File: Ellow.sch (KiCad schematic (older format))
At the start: 24 parts, among them J1 USB_C_Receptacle_USB2.0, J2 M_2_AKey_KB, J3 Conn_01x02_Female, Q1 A03407, Q2 A03407, U1 AP2112K-3.3, U2 E73-2G4M08S1C, U3 LN2054Y42AMR, Y1 32.768kHz

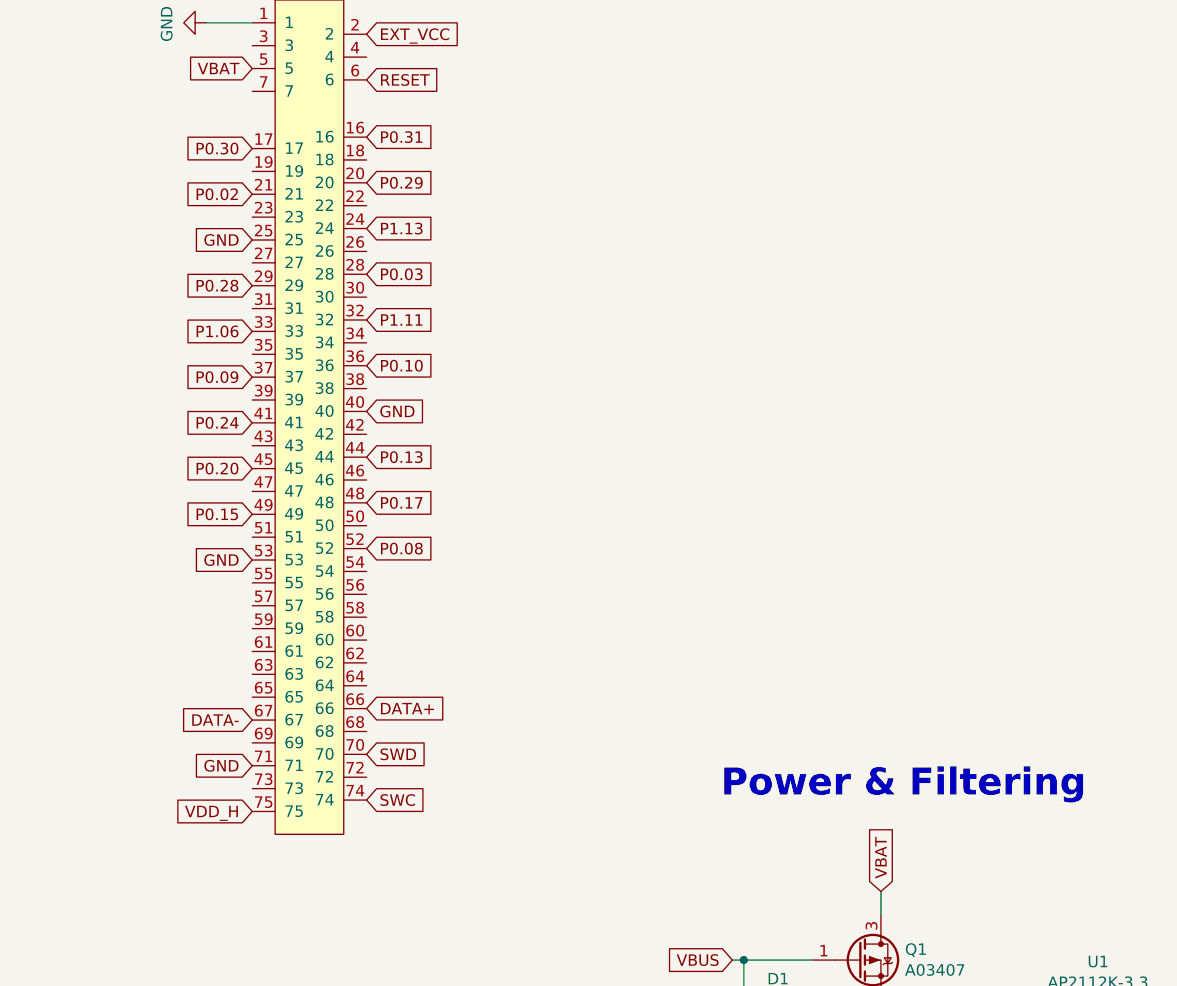
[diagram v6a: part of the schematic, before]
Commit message: no routing solution yet
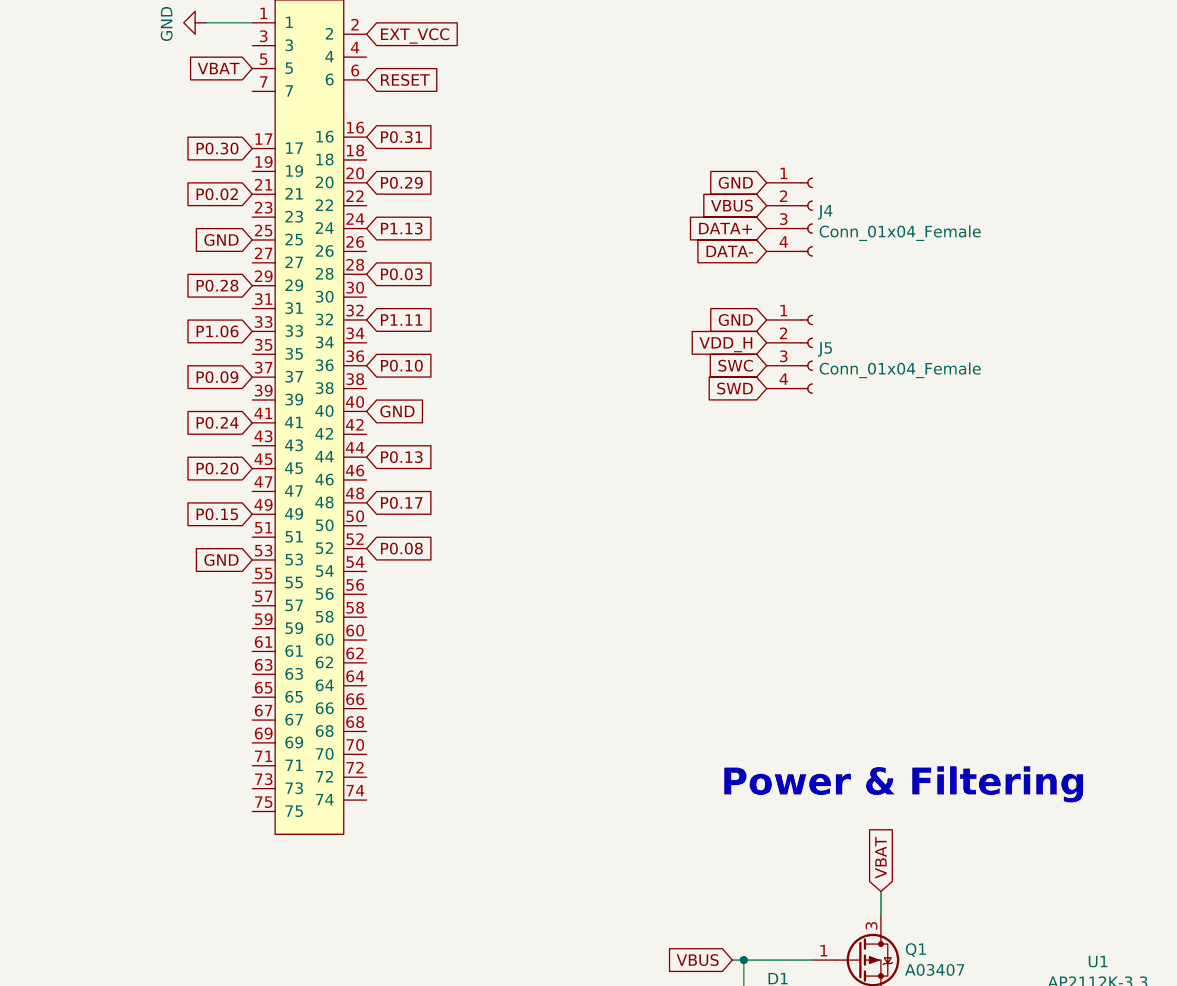
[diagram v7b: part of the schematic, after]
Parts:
- added J4, J5: Conn_01x04_Female, Connector_PinHeader_2.54mm:PinHeader_1x04_P2.54mm_Vertical, symbol Connector:Conn_01x04_Female
- J3: footprint Connector_PinHeader_1.27mm:PinHeader_1x02_P1.27mm_Vertical -> Connector_PinHeader_2.54mm:PinHeader_1x02_P2.54mm_Vertical
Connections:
- net DATA+: now also J4.3 (Pin_3); no longer J2.66
- net DATA-: now also J4.4 (Pin_4); no longer J2.67
- net GND: now also J4.1 (Pin_1), J5.1 (Pin_1); no longer J2.71
- net SWC: now also J5.3 (Pin_3); no longer J2.74
- net SWD: now also J5.4 (Pin_4); no longer J2.70
- net VBUS: now also J4.2 (Pin_2)
- net VDD_H: now also J5.2 (Pin_2); no longer J2.75
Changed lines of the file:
@@
 F 0 "J3" H 7428 6076 50  0000 L CNN
 F 1 "Conn_01x02_Female" H 7428 5985 50  0000 L CNN
-F 2 "Connector_PinHeader_1.27mm:PinHeader_1x02_P1.27mm_Vertical" H 7400 6100 50  0001 C CNN
+F 2 "Connector_PinHeader_2.54mm:PinHeader_1x02_P2.54mm_Vertical" H 7400 6100 50  0001 C CNN
 F 3 "~" H 7400 6100 50  0001 C CNN
 	1    7400 6100
@@
 Text GLabel 7150 3500 2    50   Input ~ 0
 P0.08
-Text GLabel 6650 4450 0    50   Input ~ 0
+Text GLabel 8900 2500 0    50   Input ~ 0
 GND
 Text GLabel 6650 3550 0    50   Input ~ 0
 GND
-Text GLabel 6650 4650 0    50   Input ~ 0
+Text GLabel 8900 2600 0    50   Input ~ 0
 VDD_H
-Text GLabel 7150 4600 2    50   Input ~ 0
+Text GLabel 8900 2700 0    50   Input ~ 0
 SWC
-Text GLabel 7150 4400 2    50   Input ~ 0
+Text GLabel 8900 2800 0    50   Input ~ 0
 SWD
-Text GLabel 7150 4200 2    50   Input ~ 0
+Text GLabel 8900 2100 0    50   Input ~ 0
 DATA+
-Text GLabel 6650 4250 0    50   Input ~ 0
+Text GLabel 8900 2200 0    50   Input ~ 0
 DATA-
 Text GLabel 3600 5500 2    50   Input ~ 0
@@
 Wire Wire Line
 	1750 6650 1800 6650
+$Comp
+L Connector:Conn_01x04_Female J5
+U 1 1 5FDB4AEC
+P 9100 2600
+F 0 "J5" H 9128 2576 50  0000 L CNN
+F 1 "Conn_01x04_Female" H 9128 2485 50  0000 L CNN
+F 2 "Connector_PinHeader_2.54mm:PinHeader_1x04_P2.54mm_Vertical" H 9100 2600 50  0001 C CNN
+F 3 "~" H 9100 2600 50  0001 C CNN
+	1    9100 2600
+	1    0    0    -1
+$EndComp
+$Comp
+L Connector:Conn_01x04_Female J4
+U 1 1 5FDB58A8
+P 9100 2000
+F 0 "J4" H 9128 1976 50  0000 L CNN
+F 1 "Conn_01x04_Female" H 9128 1885 50  0000 L CNN
+F 2 "Connector_PinHeader_2.54mm:PinHeader_1x04_P2.54mm_Vertical" H 9100 2000 50  0001 C CNN
+F 3 "~" H 9100 2000 50  0001 C CNN
+	1    9100 2000
+	1    0    0    -1
+$EndComp
+Text GLabel 8900 1900 0    50   Input ~ 0
+GND
+Text GLabel 8900 2000 0    50   Input ~ 0
+VBUS
 $EndSCHEMATC

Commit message: prelim routing
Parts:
- J4, J5: footprint Connector_PinHeader_2.54mm:PinHeader_1x04_P2.54mm_Vertical -> ellow:PinHeader_1x04_P2.54mm_Vertical_small
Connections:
- net BATTERY_MEASURE: now also U2.8 (P0.29/AIN5); no longer U2.18 (P0.04/AIN2)
- net EXT_VCC_CONTROL: now also U2.9 (P0.31/AIN7); no longer U2.17 (P1.09)
- net GND: now also J2.16, J2.17; no longer J2.25, J2.40, J2.53
- net P0.02: no longer J2.21
- net P0.03: no longer J2.28
- net P0.08: no longer J2.52
- net P0.09: now also J2.70; no longer J2.37
- net P0.10: now also J2.74; no longer J2.36
- net P0.13: now also J2.54; no longer J2.44
- net P0.15: now also J2.47; no longer J2.49
- net P0.17: now also J2.51; no longer J2.48
- net P0.20: now also J2.55; no longer J2.45
- net P0.22: now also J2.59
- net P0.24: now also J2.58; no longer J2.41
- net P0.28: no longer J2.29
- net P1.00: now also J2.63
- net P1.02: now also J2.67
- net P1.04: now also J2.71
- net P1.06: now also J2.75; no longer J2.33
- net P1.11: no longer J2.32
- net P1.13: no longer J2.24
- net PROG: now also U2.10 (P0.30/AIN6); no longer U2.15 (P0.05/AIN3)
- net RESET: now also J2.42; no longer J2.6
- net SWC: now also J5.4 (Pin_4); no longer J5.3 (Pin_3)
- net SWD: now also J5.3 (Pin_3); no longer J5.4 (Pin_4)
- net at U2.2 (P1.10): no longer D3.2 (A)
- net 90.07 renamed P0.07
- net P0.07: now also D3.2 (A)
- net P0.29: no longer names the net of J2.20
- net P0.29: no longer U2.8 (P0.29/AIN5)
- removed net P0.30: J2.17, U2.10 (P0.30/AIN6)
- removed net P0.31: J2.16, U2.9 (P0.31/AIN7)
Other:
- moved on the sheet: D3, R9
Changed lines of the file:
@@
 Text GLabel 2550 4250 1    50   Input ~ 0
 VDD_H
-Text GLabel 2650 4250 1    50   Input ~ 0
+Text GLabel 3600 5600 2    50   Input ~ 0
 BATTERY_MEASURE
-Text GLabel 2750 4250 1    50   Input ~ 0
+Text GLabel 3600 5500 2    50   Input ~ 0
 EXT_VCC_CONTROL
-Text GLabel 2950 4250 1    50   Input ~ 0
+Text GLabel 3600 5400 2    50   Input ~ 0
 PROG
-Wire Wire Line
-	2950 4350 2950 4250
-Wire Wire Line
-	2750 4350 2750 4250
-Wire Wire Line
-	2650 4400 2650 4250
 Wire Wire Line
 	2550 4350 2550 4250
@@
 	6650 1200 6450 1200
 $Comp
-L Device:LED D3
-U 1 1 5FC73EC6
-P 4150 6200
-F 0 "D3" H 4143 6417 50  0000 C CNN
-F 1 "LED" H 4143 6326 50  0000 C CNN
-F 2 "LED_SMD:LED_0603_1608Metric" H 4150 6200 50  0001 C CNN
-F 3 "~" H 4150 6200 50  0001 C CNN
-	1    4150 6200
-	-1   0    0    1
-$EndComp
-$Comp
-L Device:R_Small R9
-U 1 1 5FC73ECC
-P 4450 6200
-F 0 "R9" V 4254 6200 50  0000 C CNN
-F 1 "10k" V 4345 6200 50  0000 C CNN
-F 2 "Resistor_SMD:R_0603_1608Metric_Pad0.98x0.95mm_HandSolder" H 4450 6200 50  0001 C CNN
-F 3 "~" H 4450 6200 50  0001 C CNN
-	1    4450 6200
-	0    -1   -1   0
-$EndComp
-Wire Wire Line
-	4300 6200 4350 6200
-$Comp
-L power:GND #PWR0114
-U 1 1 5FC76B15
-P 4650 6200
-F 0 "#PWR0114" H 4650 5950 50  0001 C CNN
-F 1 "GND" H 4655 6027 50  0000 C CNN
-F 2 "" H 4650 6200 50  0001 C CNN
-F 3 "" H 4650 6200 50  0001 C CNN
-	1    4650 6200
-	1    0    0    -1
-$EndComp
-Wire Wire Line
-	4550 6200 4650 6200
-$Comp
 L Mechanical:MountingHole H1
 U 1 1 5FCBB591
@@
 Text Notes 6550 5900 0    118  ~ 24
 Battery Connection
-Wire Wire Line
-	3600 6200 4000 6200
 Wire Wire Line
 	3600 5900 4650 5900
@@
 Text GLabel 3600 5700 2    50   Input ~ 0
 P0.02
-Text GLabel 3600 5600 2    50   Input ~ 0
-P0.29
-Text GLabel 7150 1450 2    50   Input ~ 0
+Text GLabel 7150 3000 2    50   Input ~ 0
 RESET
 Text GLabel 7150 1250 2    50   Input ~ 0
 EXT_VCC
 Text GLabel 6650 1750 0    50   Input ~ 0
-P0.30
-Text GLabel 7150 1700 2    50   Input ~ 0
-P0.31
-Text GLabel 7150 1900 2    50   Input ~ 0
-P0.29
-Text GLabel 6650 1950 0    50   Input ~ 0
-P0.02
-Text GLabel 7150 2100 2    50   Input ~ 0
-P1.13
-Text GLabel 6650 2150 0    50   Input ~ 0
 GND
-Text GLabel 7150 2300 2    50   Input ~ 0
-P0.03
-Text GLabel 6650 2350 0    50   Input ~ 0
-P0.28
-Text GLabel 7150 2500 2    50   Input ~ 0
-P1.11
-Text GLabel 6650 2550 0    50   Input ~ 0
+Text GLabel 6650 4650 0    50   Input ~ 0
 P1.06
-Text GLabel 7150 2700 2    50   Input ~ 0
+Text GLabel 7150 4600 2    50   Input ~ 0
 P0.10
-Text GLabel 7150 2900 2    50   Input ~ 0
-GND
-Text GLabel 6650 2750 0    50   Input ~ 0
-P0.09
-Text GLabel 6650 2950 0    50   Input ~ 0
+Text GLabel 7150 3800 2    50   Input ~ 0
 P0.24
-Text GLabel 7150 3100 2    50   Input ~ 0
-P0.13
-Text GLabel 6650 3150 0    50   Input ~ 0
-P0.20
-Text GLabel 7150 3300 2    50   Input ~ 0
+Text GLabel 6650 3450 0    50   Input ~ 0
 P0.17
-Text GLabel 6650 3350 0    50   Input ~ 0
-P0.15
-Text GLabel 7150 3500 2    50   Input ~ 0
-P0.08
 Text GLabel 8900 2500 0    50   Input ~ 0
-GND
-Text GLabel 6650 3550 0    50   Input ~ 0
 GND
 Text GLabel 8900 2600 0    50   Input ~ 0
 VDD_H
+Text GLabel 8900 2800 0    50   Input ~ 0
+SWC
 Text GLabel 8900 2700 0    50   Input ~ 0
-SWC
-Text GLabel 8900 2800 0    50   Input ~ 0
 SWD
 Text GLabel 8900 2100 0    50   Input ~ 0
@@
 Text GLabel 8900 2200 0    50   Input ~ 0
 DATA-
-Text GLabel 3600 5500 2    50   Input ~ 0
-P0.31
-Text GLabel 3600 5400 2    50   Input ~ 0
-P0.30
 Text GLabel 3250 4400 1    50   Input ~ 0
 P0.26
@@
 Text GLabel 2450 4400 1    50   Input ~ 0
 P0.12
-Text GLabel 2250 4400 1    50   Input ~ 0
-90.07
 Text GLabel 1750 5250 0    50   Input ~ 0
 P0.15
@@
 F 0 "J5" H 9128 2576 50  0000 L CNN
 F 1 "Conn_01x04_Female" H 9128 2485 50  0000 L CNN
-F 2 "Connector_PinHeader_2.54mm:PinHeader_1x04_P2.54mm_Vertical" H 9100 2600 50  0001 C CNN
+F 2 "ellow:PinHeader_1x04_P2.54mm_Vertical_small" H 9100 2600 50  0001 C CNN
 F 3 "~" H 9100 2600 50  0001 C CNN
 	1    9100 2600
@@
 F 0 "J4" H 9128 1976 50  0000 L CNN
 F 1 "Conn_01x04_Female" H 9128 1885 50  0000 L CNN
-F 2 "Connector_PinHeader_2.54mm:PinHeader_1x04_P2.54mm_Vertical" H 9100 2000 50  0001 C CNN
+F 2 "ellow:PinHeader_1x04_P2.54mm_Vertical_small" H 9100 2000 50  0001 C CNN
 F 3 "~" H 9100 2000 50  0001 C CNN
 	1    9100 2000
@@
 Text GLabel 8900 2000 0    50   Input ~ 0
 VBUS
+Text GLabel 6650 4250 0    50   Input ~ 0
+P1.02
+Text GLabel 6650 4050 0    50   Input ~ 0
+P1.00
+Text GLabel 6650 3850 0    50   Input ~ 0
+P0.22
+Text GLabel 7150 3600 2    50   Input ~ 0
+P0.13
+Text GLabel 6650 3250 0    50   Input ~ 0
+P0.15
+$Comp
+L Device:LED D3
+U 1 1 5FC73EC6
+P 4400 4200
+F 0 "D3" H 4393 4417 50  0000 C CNN
+F 1 "LED" H 4393 4326 50  0000 C CNN
+F 2 "LED_SMD:LED_0603_1608Metric" H 4400 4200 50  0001 C CNN
+F 3 "~" H 4400 4200 50  0001 C CNN
+	1    4400 4200
+	-1   0    0    1
+$EndComp
+Wire Wire Line
+	4800 4200 4900 4200
+$Comp
+L power:GND #PWR0114
+U 1 1 5FC76B15
+P 4900 4200
+F 0 "#PWR0114" H 4900 3950 50  0001 C CNN
+F 1 "GND" H 4905 4027 50  0000 C CNN
+F 2 "" H 4900 4200 50  0001 C CNN
+F 3 "" H 4900 4200 50  0001 C CNN
+	1    4900 4200
+	1    0    0    -1
+$EndComp
+Wire Wire Line
+	4550 4200 4600 4200
+$Comp
+L Device:R_Small R9
+U 1 1 5FC73ECC
+P 4700 4200
+F 0 "R9" V 4504 4200 50  0000 C CNN
+F 1 "10k" V 4595 4200 50  0000 C CNN
+F 2 "Resistor_SMD:R_0603_1608Metric_Pad0.98x0.95mm_HandSolder" H 4700 4200 50  0001 C CNN
+F 3 "~" H 4700 4200 50  0001 C CNN
+	1    4700 4200
+	0    -1   -1   0
+$EndComp
+Text GLabel 2250 4400 1    50   Input ~ 0
+P0.07
+Text GLabel 4250 4200 0    50   Input ~ 0
+P0.07
+Text GLabel 6650 3650 0    50   Input ~ 0
+P0.20
+Text GLabel 7150 4400 2    50   Input ~ 0
+P0.09
+Text GLabel 6650 4450 0    50   Input ~ 0
+P1.04
+Text GLabel 7150 1700 2    50   Input ~ 0
+GND
 $EndSCHEMATC
